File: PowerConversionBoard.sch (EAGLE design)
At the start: 33 parts, among them Q1 MOSFET_PCH-NDS8434, U3 AZ1117EH-3.3TRG1

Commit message: routed the board
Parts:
- removed U$2: DIST_TO_CONV, Dist_To_Conv_Connector:DIST_TO_CONV
- added U$3: CON2DIST, Dist_Convert_Connector:CON2DIST
- CIN: value 47uF -> 3.33uF
- COUT: value 150uF -> 100uF
- renumbered C24 to COUT, U$4 to D1, U$7 to L1
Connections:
- net +3.3V: now also U$3.VOUT+_3; no longer U$2.3V, U$2.48V
- net +48V: now also U$3.VIN+
- net +5V: now also U$3.VOUT+_5; no longer U$2.5V_1, U$2.5V_2, U$2.5V_3, U$2.5V_4
- net GND: now also U$3.VIN-, U$3.VOUT-; no longer U$2.GND_1, U$2.GND_2, U$2.GND_3, U$2.GND_4

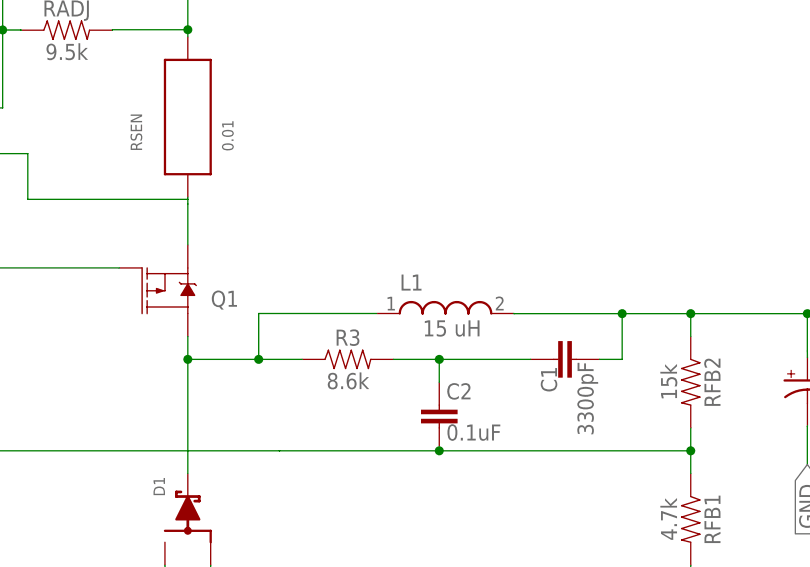
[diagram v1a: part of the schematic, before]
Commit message: wrong inductor previously. oops
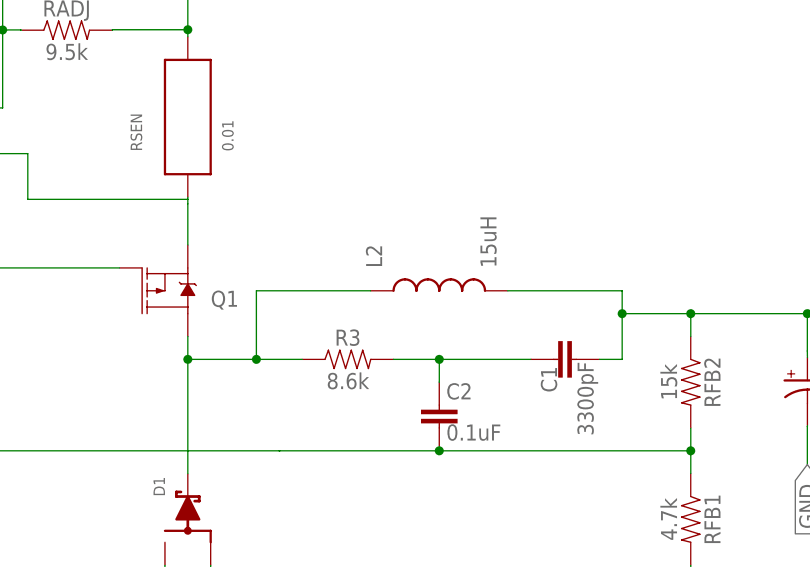
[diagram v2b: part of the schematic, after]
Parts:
- removed L1: HCM1305, HCM1305:HCM1305
- added L2: 15uH, Inductor_15uH - hcma1305:HCMA1305
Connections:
- net +5V: now also L2.2; no longer L1.2
- net N$10: now also L2.1; no longer L1.1
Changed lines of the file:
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@@
 <?xml version="1.0" encoding="utf-8"?>
 <!DOCTYPE eagle SYSTEM "eagle.dtd">
-<eagle version="9.6.2">
+<eagle version="9.5.0">
 <drawing>
 <settings>
@@
 <setting verticaltext="up"/>
 </settings>
-<grid distance="0.1" unitdist="inch" unit="inch" style="lines" multiple="1" display="yes" altdistance="0.01" altunitdist="inch" altunit="inch"/>
+<grid distance="0.1" unitdist="inch" unit="inch" style="lines" multiple="1" display="no" altdistance="0.01" altunitdist="inch" altunit="inch"/>
 <layers>
 <layer number="1" name="Top" color="4" fill="1" visible="no" active="no"/>
@@
 <part name="R1" library="SparkFun-Resistors" library_urn="urn:adsk.eagle:library:532" deviceset="1.6KOHM" device="-0603-1/10W-1%" package3d_urn="urn:adsk.eagle:package:39650/1" value="1.2 Ohms"/>
 <part name="COUT" library="PowerComponents" deviceset="C-TANTALUM(10UF_150UF)" device="" value="100uF"/>
-<part name="L1" library="HCM1305" deviceset="HCM1305" device=""/>
 <part name="D1" library="PowerComponents" deviceset="SWITCHMODE_SCHOTTKY" device=""/>
 <part name="RSEN" library="INA4181A4" deviceset="CSS2H-2512" device="" value="0.01"/>
 <part name="U$3" library="Dist_Convert_Connector" deviceset="CON2DIST" device=""/>
+<part name="L2" library="Inductor_15uH - hcma1305" deviceset="HCMA1305" device="" package3d_urn="urn:adsk.eagle:package:24201702/2" value="15uH"/>
 </parts>
 <sheets>
@@
 <attribute name="VALUE" x="313.701278125" y="166.184990625" size="1.778" layer="96"/>
 </instance>
-<instance part="L1" gate="G$1" x="272.470953125" y="177.816271875" smashed="yes" rot="R90">
-<attribute name="NAME" x="267.375334375" y="180.36408125" size="1.78346875" layer="95"/>
-</instance>
 <instance part="D1" gate="G$1" x="243.84" y="157.48" smashed="yes" rot="R90">
 <attribute name="NAME" x="241.3" y="157.48" size="1.27" layer="95" rot="R90"/>
@@
 <instance part="U$3" gate="G$1" x="165.481" y="-111.125" smashed="yes">
 <attribute name="NAME" x="162.941" y="-105.283" size="1.27" layer="95"/>
+</instance>
+<instance part="L2" gate="G$1" x="271.78" y="180.34" smashed="yes" rot="R90">
+<attribute name="NAME" x="265.43" y="182.88" size="1.778" layer="95" rot="R90"/>
+<attribute name="VALUE" x="278.13" y="182.88" size="1.778" layer="96" rot="R90"/>
 </instance>
 </instances>
@@
 </segment>
 <segment>
-<wire x1="280.090953125" y1="177.8" x2="292.1" y2="177.8" width="0.1524" layer="91"/>
 <pinref part="C1" gate="G$1" pin="1"/>
 <wire x1="292.1" y1="177.8" x2="292.1" y2="172.72" width="0.1524" layer="91"/>
@@
 <junction x="299.72" y="177.8"/>
 <label x="317.5" y="177.8" size="1.778" layer="95" xref="yes"/>
-<pinref part="L1" gate="G$1" pin="2"/>
 <wire x1="312.674" y1="177.8" x2="317.5" y2="177.8" width="0.1524" layer="91"/>
-<wire x1="280.090953125" y1="177.8" x2="280.090953125" y2="177.816271875" width="0.1524" layer="91"/>
 <pinref part="COUT" gate="G$1" pin="+"/>
 <wire x1="312.674" y1="177.8" x2="312.674" y2="173.652590625" width="0.1524" layer="91"/>
 <wire x1="312.674" y1="173.652590625" x2="312.685278125" y2="172.915990625" width="0.1524" layer="91"/>
 <junction x="312.674" y="177.8"/>
+<pinref part="L2" gate="G$1" pin="2"/>
+<wire x1="292.1" y1="177.8" x2="292.1" y2="180.34" width="0.1524" layer="91"/>
+<wire x1="292.1" y1="180.34" x2="279.4" y2="180.34" width="0.1524" layer="91"/>
 </segment>
 <segment>
@@
 <wire x1="243.84" y1="175.26" x2="243.84" y2="172.72" width="0.1524" layer="91"/>
 <pinref part="R3" gate="G$1" pin="1"/>
-<wire x1="243.84" y1="172.72" x2="251.714" y2="172.72" width="0.1524" layer="91"/>
-<wire x1="251.714" y1="172.72" x2="256.54" y2="172.72" width="0.1524" layer="91"/>
+<wire x1="243.84" y1="172.72" x2="251.46" y2="172.72" width="0.1524" layer="91"/>
+<wire x1="251.46" y1="172.72" x2="256.54" y2="172.72" width="0.1524" layer="91"/>
 <wire x1="243.84" y1="172.72" x2="243.84" y2="160.02" width="0.1524" layer="91"/>
 <junction x="243.84" y="172.72"/>
-<pinref part="L1" gate="G$1" pin="1"/>
-<wire x1="251.714" y1="172.72" x2="251.714" y2="177.816271875" width="0.1524" layer="91"/>
-<wire x1="251.714" y1="177.816271875" x2="264.850953125" y2="177.816271875" width="0.1524" layer="91"/>
-<junction x="251.714" y="172.72"/>
 <pinref part="D1" gate="G$1" pin="P$4"/>
-</segment>
-</net>
+<pinref part="L2" gate="G$1" pin="1"/>
+<wire x1="251.46" y1="172.72" x2="251.46" y2="180.34" width="0.1524" layer="91"/>
+<wire x1="251.46" y1="180.34" x2="264.16" y2="180.34" width="0.1524" layer="91"/>
+<junction x="251.46" y="172.72"/>
+</segment>
+</net>

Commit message: Finished all the routing
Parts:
- RADJ: value 9.5k -> 1.8k
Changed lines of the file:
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@@
 <?xml version="1.0" encoding="utf-8"?>
 <!DOCTYPE eagle SYSTEM "eagle.dtd">
-<eagle version="9.5.0">
+<eagle version="9.6.2">
 <drawing>
 <settings>
@@
 <part name="Q1" library="SparkFun-DiscreteSemi" library_urn="urn:adsk.eagle:library:514" deviceset="MOSFET_PCH" device="-NDS8434" package3d_urn="urn:adsk.eagle:package:38445/1" value=""/>
 <part name="RFB1" library="SparkFun-Resistors" library_urn="urn:adsk.eagle:library:532" deviceset="RESISTOR" device="0603" package3d_urn="urn:adsk.eagle:package:39650/1" value="4.7k"/>
-<part name="RADJ" library="SparkFun-Resistors" library_urn="urn:adsk.eagle:library:532" deviceset="RESISTOR" device="0603" package3d_urn="urn:adsk.eagle:package:39650/1" value="9.5k"/>
+<part name="RADJ" library="SparkFun-Resistors" library_urn="urn:adsk.eagle:library:532" deviceset="RESISTOR" device="0603" package3d_urn="urn:adsk.eagle:package:39650/1" value="1.8k"/>
 <part name="RFB2" library="SparkFun-Resistors" library_urn="urn:adsk.eagle:library:532" deviceset="RESISTOR" device="0603" package3d_urn="urn:adsk.eagle:package:39650/1" value="15k"/>
 <part name="R3" library="SparkFun-Resistors" library_urn="urn:adsk.eagle:library:532" deviceset="RESISTOR" device="0603" package3d_urn="urn:adsk.eagle:package:39650/1" value="8.6k"/>

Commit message: Rough draft of the new and improved board finished; need to work out wires connecting to polygons and probably clean up the test points; there are also a few strange wiring places that need to be cleaned up
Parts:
- removed COUPLE: 1nF, SparkFun-Capacitors:1.0NF/1000PF-0603-50V-10%
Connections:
- net +5V: no longer COUPLE.1
- net GND: no longer COUPLE.2
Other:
- note added: "Buck Controller"
- note added: "Distribution Connector"
- note added: "Linear Regulator"
- note added: "Test Diodes"
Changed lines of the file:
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@@
 <part name="U3" library="Linear Regulator - AZ1117EH-3.3TRG1" deviceset="AZ1117EH-3.3TRG1" device=""/>
 <part name="U$1" library="Buck_Controller" deviceset="LM5085" device=""/>
-<part name="COUPLE" library="SparkFun-Capacitors" library_urn="urn:adsk.eagle:library:510" deviceset="1.0NF/1000PF" device="-0603-50V-10%" package3d_urn="urn:adsk.eagle:package:37414/1" value="1nF"/>
 <part name="Q1" library="SparkFun-DiscreteSemi" library_urn="urn:adsk.eagle:library:514" deviceset="MOSFET_PCH" device="-NDS8434" package3d_urn="urn:adsk.eagle:package:38445/1" value=""/>
 <part name="RFB1" library="SparkFun-Resistors" library_urn="urn:adsk.eagle:library:532" deviceset="RESISTOR" device="0603" package3d_urn="urn:adsk.eagle:package:39650/1" value="4.7k"/>
@@
 <text x="246.38" y="106.68" size="1.778" layer="95">Test Points</text>
 <text x="213.36" y="106.68" size="1.778" layer="95">Pins</text>
+<text x="101.6" y="101.6" size="1.778" layer="91">Linear Regulator</text>
+<text x="185.42" y="218.44" size="1.778" layer="91">Buck Controller</text>
+<text x="66.04" y="223.52" size="1.778" layer="91">Test Diodes</text>
+<text x="226.06" y="114.3" size="1.778" layer="91">Test Points</text>
+<text x="162.56" y="-93.98" size="1.778" layer="91">Distribution Connector</text>
 </plain>
 <instances>
@@
 </instance>
 <instance part="U$1" gate="G$1" x="193.04" y="195.58" smashed="yes"/>
-<instance part="COUPLE" gate="G$1" x="91.44" y="73.66" smashed="yes">
-<attribute name="NAME" x="92.964" y="76.581" size="1.778" layer="95" font="vector"/>
-<attribute name="VALUE" x="92.964" y="71.501" size="1.778" layer="96" font="vector"/>
-</instance>
 <instance part="Q1" gate="G$1" x="241.3" y="180.34" smashed="yes" rot="MR180">
 <attribute name="NAME" x="246.38" y="180.34" size="1.778" layer="95" font="vector" rot="MR180"/>
@@
 <wire x1="119.38" y1="86.36" x2="127" y2="86.36" width="0.1524" layer="91"/>
 <label x="129.54" y="86.36" size="1.778" layer="95" xref="yes"/>
-<pinref part="COUPLE" gate="G$1" pin="2"/>
 <wire x1="127" y1="86.36" x2="129.54" y2="86.36" width="0.1524" layer="91"/>
-<wire x1="91.44" y1="71.12" x2="91.44" y2="66.04" width="0.1524" layer="91"/>
-<wire x1="91.44" y1="66.04" x2="127" y2="66.04" width="0.1524" layer="91"/>
-<wire x1="127" y1="66.04" x2="127" y2="86.36" width="0.1524" layer="91"/>
+<wire x1="127" y1="48.26" x2="127" y2="86.36" width="0.1524" layer="91"/>
 <junction x="127" y="86.36"/>
 <pinref part="R1" gate="G$1" pin="1"/>
 <wire x1="152.4" y1="55.88" x2="152.4" y2="48.26" width="0.1524" layer="91"/>
-<wire x1="127" y1="66.04" x2="127" y2="48.26" width="0.1524" layer="91"/>
 <wire x1="127" y1="48.26" x2="152.4" y2="48.26" width="0.1524" layer="91"/>
-<junction x="127" y="66.04"/>
 </segment>
 <segment>
@@
 <segment>
 <pinref part="U3" gate="G$1" pin="IN"/>
-<wire x1="99.06" y1="91.44" x2="91.44" y2="91.44" width="0.1524" layer="91"/>
+<wire x1="99.06" y1="91.44" x2="88.9" y2="91.44" width="0.1524" layer="91"/>
 <label x="88.9" y="91.44" size="1.778" layer="95" rot="R180" xref="yes"/>
-<pinref part="COUPLE" gate="G$1" pin="1"/>
-<wire x1="91.44" y1="91.44" x2="88.9" y2="91.44" width="0.1524" layer="91"/>
-<wire x1="91.44" y1="91.44" x2="91.44" y2="78.74" width="0.1524" layer="91"/>
-<junction x="91.44" y="91.44"/>
-</segment>
-<segment>
+</segment>
+<segment>
